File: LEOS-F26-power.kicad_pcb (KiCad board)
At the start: 4 copper layers, 100 x 100 mm, 71 parts, among them J1 MicroFit_1x4, J2 MicroFit_1x4, J3 Power Input, J4 5V, J5 5V, J6 5V, J7 1-18V, J8 1-18V, J9 1-18V, U1 MCP2518FD, U2 MCP2562FD, U3 TPS54540BDDA, U4 TPS16630PWPR, U5 TPS54540BDDA, U6 MCP41HV51-104E/MQ, Y1 40 MHz

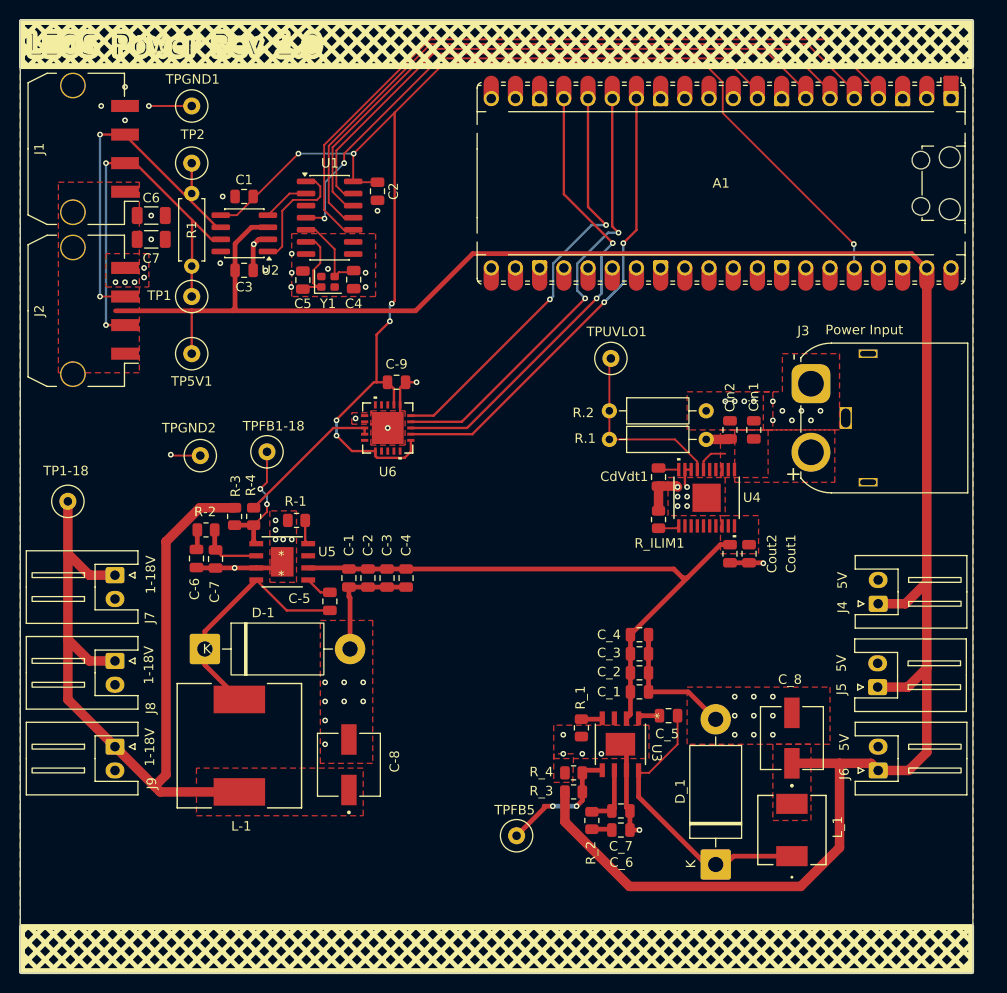
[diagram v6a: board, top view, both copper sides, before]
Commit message: Change routing to include l2 power layer to rearrange buck layout
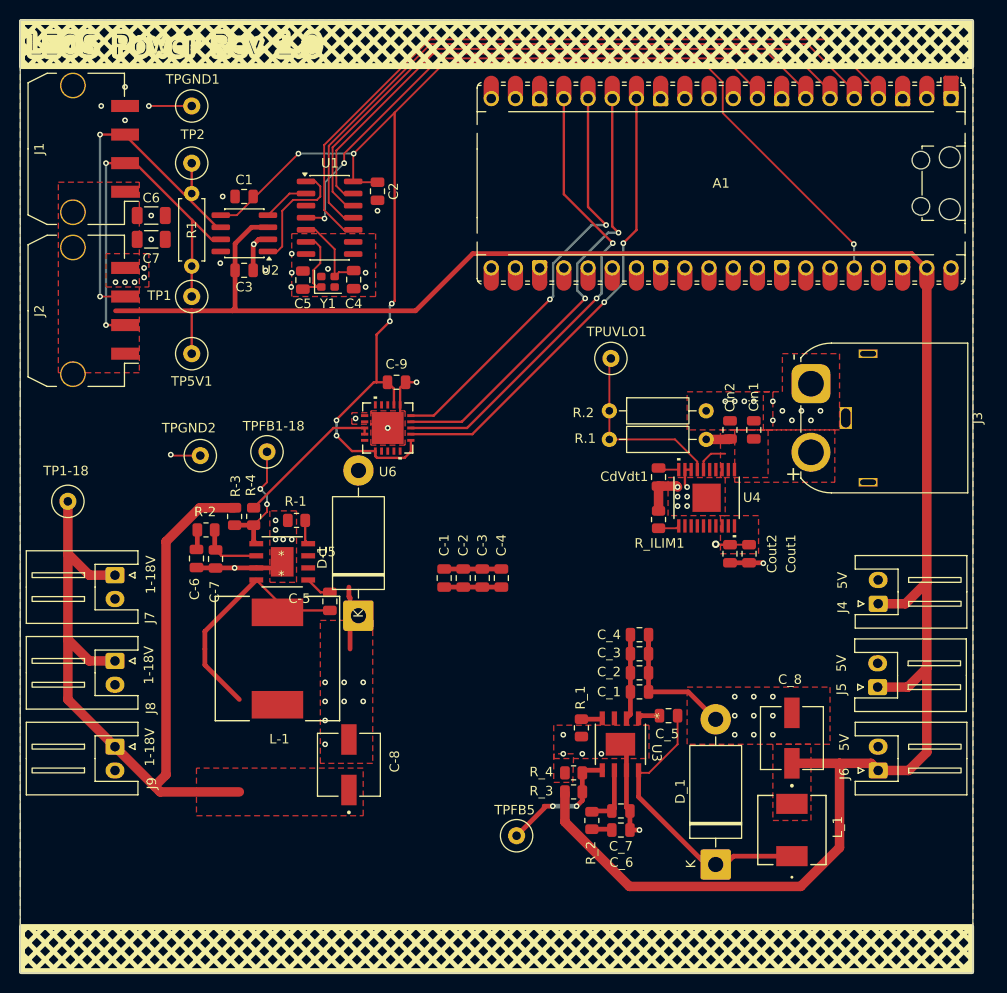
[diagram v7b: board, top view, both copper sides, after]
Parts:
- J3: footprint Connector_AMASS:AMASS_XT60IPW-M_1x03_P7.20mm_Horizontal -> LEOS:AMASS_XT60IPW-M_1x03_P7.20mm_Horizontal
- R.1: value 150k -> 160k
- moved D-1 16.5 mm to (135.5, 112.5), turned to 90 degrees
- moved C-1 10.0 mm to (144.5, 108.5)
- moved C-2 10.0 mm to (146.5, 108.5)
- moved C-3 10.0 mm to (148.5, 108.5)
- moved C-4 10.0 mm to (150.5, 108.5)
- moved L-1 9.98 mm to (127.0, 117.0)
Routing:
- net VPP: track 63.0 -> 19.6 mm, vias 0 -> 1
- net GND: track 78.1 -> 71.5 mm
- net Net-(D-1-K): track 25.3 -> 31.9 mm
- added copper zone on In2.Cu, net +5V
- added copper zone on In2.Cu, net VDC
- added copper zone on In2.Cu, net VDD
- added copper zone on In2.Cu, net VPP

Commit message: updates to routing and digital pot
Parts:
- R-4: value 25.5k -> 26.1k
- U6: value MCP41HV51-104E/MQ -> MCP41100T-I/SN; footprint LEOS:QFN20_5x5MC_MCH -> LEOS:SOIC8-N_MC_MCH
- moved L_1 13.2 mm to (170.4, 127.1), turned to 0 degrees
- moved C-8 11.1 mm to (123.6, 130.1), turned to -90 degrees
- moved D_1 6.41 mm to (167.8, 134.9), turned to 0 degrees
- moved C-1 5.25 mm to (141.8, 104.0)
- moved C-2 5.25 mm to (143.8, 104.0)
- moved C-3 5.25 mm to (145.8, 104.0)
- moved C-4 5.25 mm to (147.8, 104.0)
- moved U6 4.38 mm to (142.9, 93.5), turned to 90 degrees
- moved L-1 3.43 mm to (123.6, 117.5)
- moved C-9 2.58 mm to (142.1, 88.4)
- moved C_8 2.10 mm to (179.1, 124.5)
- moved C_5 1.38 mm to (168.5, 121.7)
- moved D-1 0.99 mm to (136.3, 111.9)
- moved C-5 0.73 mm to (131.8, 111.2)
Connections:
- A1 pad 16: /MISO1 -> unconnected-(A1-GPIO12-Pad16)
- R-3 pad 2: /1-18V Power/POT -> GND
- U6 pad 1: VDD -> /CS1
- U6 pad 3: /CS1 -> /MOSI1
- U6 pad 4: /MOSI1 -> GND
- U6 pad 5: /MISO1 -> GND
- U6 pad 7: VDD -> GND
- U6 pad 8: unconnected-(U6-NC-Pad8) -> VDD
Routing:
- net VDC: track 89.4 -> 1.71 mm, vias 0 -> 21
- net +5V: track 226.7 -> 144.7 mm, vias 0 -> 16
- net /MISO1: track 44.9 -> 0.00 mm, vias 2 -> 0
- net VDD: track 141.7 -> 123.4 mm, vias 7 -> 5
- net /1-18V Power/POT: track 15.8 -> 0.00 mm
- net VPP: track 19.6 -> 35.3 mm, vias 1 -> 10
- net Net-(D_1-K): track 29.7 -> 20.2 mm, vias 0 -> 2
- net Net-(D-1-K): track 31.9 -> 27.0 mm, vias 0 -> 3
- net GND: track 71.5 -> 75.4 mm, vias 72 -> 63
- net /MOSI1: track 47.7 -> 49.6 mm
- net /SCK1: track 48.8 -> 50.4 mm
- net Net-(U3-BOOT): track 2.31 -> 3.30 mm
- net Net-(U5-BOOT): track 2.81 -> 2.20 mm
- net /CS1: track 48.9 -> 49.5 mm
- removed copper zone on In2.Cu, net VDD
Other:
- board text added: "1-18V"
- board text added: "Input 12-24VDC"
